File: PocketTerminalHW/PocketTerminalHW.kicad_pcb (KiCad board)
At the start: 2 copper layers, 85.5 x 54 mm, 183 parts, among them J1 USB4105-GF-A, J2 DM3D-SF, J3 53261-0271, J4 Conn_01x04, J5 Conn_01x02, J6 68712414522, J7 USB4105-GF-A, J8 66011102111302, J9 Conn_01x05, Q1 BC847BDW1, SW1 K3-1391D-5MM, U1 ESP32-S3-WROOM-1, U2 CP2102N-A02-GQFN28, U3 AMS1117-3.3 / SGM2212-3.3, U4 TP4056-42-ESOP8, U5 MT3608/SX1308, U6 CC1101RGPR, Y1 3225-26M-SR

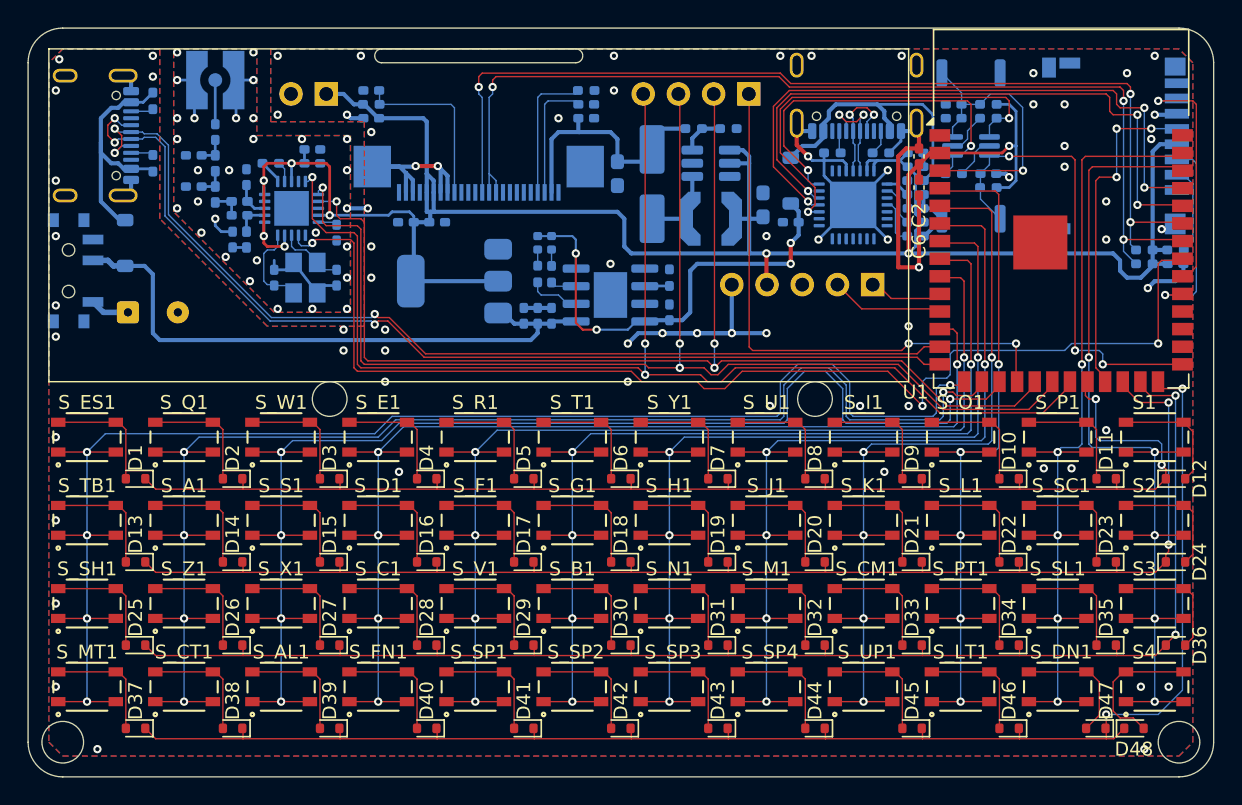
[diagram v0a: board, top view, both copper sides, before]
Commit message: Project rename and minor PCB changes
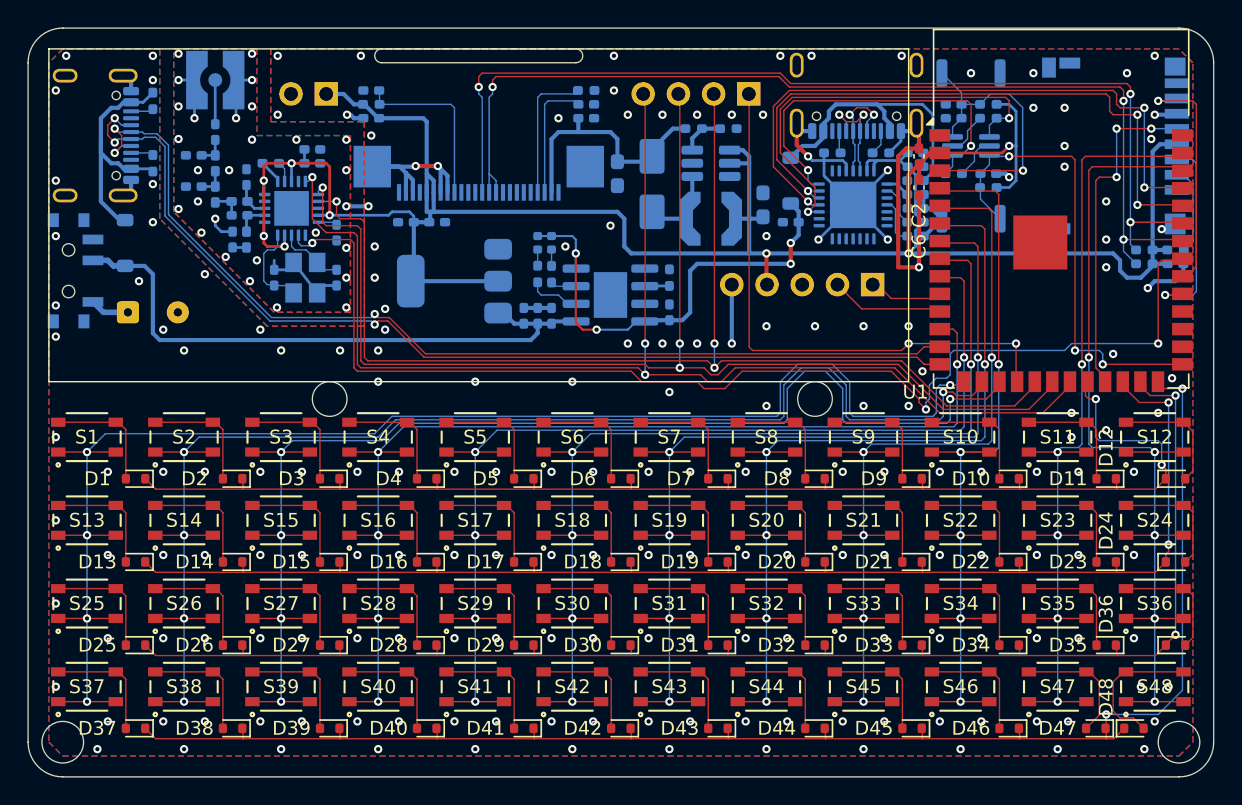
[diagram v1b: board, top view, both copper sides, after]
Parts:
- D52: footprint Diode_SMD:D_SMA_Handsoldering -> Diode_SMD:D_SMA
- J6: footprint DataSlice:68712414522 -> PocketTerminal:68712414522
- S1: renamed from S_ES1; footprint DataSlice:SW4_SKRPABE010_ALPS -> PocketTerminal:SW4_SKRPABE010_ALPS
- S10: renamed from S_O1; footprint DataSlice:SW4_SKRPABE010_ALPS -> PocketTerminal:SW4_SKRPABE010_ALPS
- S11: renamed from S_P1; footprint DataSlice:SW4_SKRPABE010_ALPS -> PocketTerminal:SW4_SKRPABE010_ALPS
- S12: renamed from S1; footprint DataSlice:SW4_SKRPABE010_ALPS -> PocketTerminal:SW4_SKRPABE010_ALPS
- S13: renamed from S_TB1; footprint DataSlice:SW4_SKRPABE010_ALPS -> PocketTerminal:SW4_SKRPABE010_ALPS
- S14: renamed from S_A1; footprint DataSlice:SW4_SKRPABE010_ALPS -> PocketTerminal:SW4_SKRPABE010_ALPS
- S15: renamed from S_S1; footprint DataSlice:SW4_SKRPABE010_ALPS -> PocketTerminal:SW4_SKRPABE010_ALPS
- S16: renamed from S_D1; footprint DataSlice:SW4_SKRPABE010_ALPS -> PocketTerminal:SW4_SKRPABE010_ALPS
- S17: renamed from S_F1; footprint DataSlice:SW4_SKRPABE010_ALPS -> PocketTerminal:SW4_SKRPABE010_ALPS
- S18: renamed from S_G1; footprint DataSlice:SW4_SKRPABE010_ALPS -> PocketTerminal:SW4_SKRPABE010_ALPS
- S19: renamed from S_H1; footprint DataSlice:SW4_SKRPABE010_ALPS -> PocketTerminal:SW4_SKRPABE010_ALPS
- S2: renamed from S_Q1; footprint DataSlice:SW4_SKRPABE010_ALPS -> PocketTerminal:SW4_SKRPABE010_ALPS
- S20: renamed from S_J1; footprint DataSlice:SW4_SKRPABE010_ALPS -> PocketTerminal:SW4_SKRPABE010_ALPS
- S21: renamed from S_K1; footprint DataSlice:SW4_SKRPABE010_ALPS -> PocketTerminal:SW4_SKRPABE010_ALPS
- S22: renamed from S_L1; footprint DataSlice:SW4_SKRPABE010_ALPS -> PocketTerminal:SW4_SKRPABE010_ALPS
- S23: renamed from S_SC1; footprint DataSlice:SW4_SKRPABE010_ALPS -> PocketTerminal:SW4_SKRPABE010_ALPS
- S24: renamed from S2; footprint DataSlice:SW4_SKRPABE010_ALPS -> PocketTerminal:SW4_SKRPABE010_ALPS
- S25: renamed from S_SH1; footprint DataSlice:SW4_SKRPABE010_ALPS -> PocketTerminal:SW4_SKRPABE010_ALPS
- S26: renamed from S_Z1; footprint DataSlice:SW4_SKRPABE010_ALPS -> PocketTerminal:SW4_SKRPABE010_ALPS
- S27: renamed from S_X1; footprint DataSlice:SW4_SKRPABE010_ALPS -> PocketTerminal:SW4_SKRPABE010_ALPS
- S28: renamed from S_C1; footprint DataSlice:SW4_SKRPABE010_ALPS -> PocketTerminal:SW4_SKRPABE010_ALPS
- S29: renamed from S_V1; footprint DataSlice:SW4_SKRPABE010_ALPS -> PocketTerminal:SW4_SKRPABE010_ALPS
- S3: renamed from S_W1; footprint DataSlice:SW4_SKRPABE010_ALPS -> PocketTerminal:SW4_SKRPABE010_ALPS
- S30: renamed from S_B1; footprint DataSlice:SW4_SKRPABE010_ALPS -> PocketTerminal:SW4_SKRPABE010_ALPS
- S31: renamed from S_N1; footprint DataSlice:SW4_SKRPABE010_ALPS -> PocketTerminal:SW4_SKRPABE010_ALPS
- S32: renamed from S_M1; footprint DataSlice:SW4_SKRPABE010_ALPS -> PocketTerminal:SW4_SKRPABE010_ALPS
- S33: renamed from S_CM1; footprint DataSlice:SW4_SKRPABE010_ALPS -> PocketTerminal:SW4_SKRPABE010_ALPS
- S34: renamed from S_PT1; footprint DataSlice:SW4_SKRPABE010_ALPS -> PocketTerminal:SW4_SKRPABE010_ALPS
- S35: renamed from S_SL1; footprint DataSlice:SW4_SKRPABE010_ALPS -> PocketTerminal:SW4_SKRPABE010_ALPS
- S36: renamed from S3; footprint DataSlice:SW4_SKRPABE010_ALPS -> PocketTerminal:SW4_SKRPABE010_ALPS
- S37: renamed from S_MT1; footprint DataSlice:SW4_SKRPABE010_ALPS -> PocketTerminal:SW4_SKRPABE010_ALPS
- S38: renamed from S_CT1; footprint DataSlice:SW4_SKRPABE010_ALPS -> PocketTerminal:SW4_SKRPABE010_ALPS
- S39: renamed from S_AL1; footprint DataSlice:SW4_SKRPABE010_ALPS -> PocketTerminal:SW4_SKRPABE010_ALPS
- S4: renamed from S_E1; footprint DataSlice:SW4_SKRPABE010_ALPS -> PocketTerminal:SW4_SKRPABE010_ALPS
- S40: renamed from S_FN1; footprint DataSlice:SW4_SKRPABE010_ALPS -> PocketTerminal:SW4_SKRPABE010_ALPS
- S41: renamed from S_SP1; footprint DataSlice:SW4_SKRPABE010_ALPS -> PocketTerminal:SW4_SKRPABE010_ALPS
- S42: renamed from S_SP2; footprint DataSlice:SW4_SKRPABE010_ALPS -> PocketTerminal:SW4_SKRPABE010_ALPS
- S43: renamed from S_SP3; footprint DataSlice:SW4_SKRPABE010_ALPS -> PocketTerminal:SW4_SKRPABE010_ALPS
- S44: renamed from S_SP4; footprint DataSlice:SW4_SKRPABE010_ALPS -> PocketTerminal:SW4_SKRPABE010_ALPS
- S45: renamed from S_UP1; footprint DataSlice:SW4_SKRPABE010_ALPS -> PocketTerminal:SW4_SKRPABE010_ALPS
- S46: renamed from S_LT1; footprint DataSlice:SW4_SKRPABE010_ALPS -> PocketTerminal:SW4_SKRPABE010_ALPS
- S47: renamed from S_DN1; footprint DataSlice:SW4_SKRPABE010_ALPS -> PocketTerminal:SW4_SKRPABE010_ALPS
- S48: renamed from S4; footprint DataSlice:SW4_SKRPABE010_ALPS -> PocketTerminal:SW4_SKRPABE010_ALPS
- S5: renamed from S_R1; footprint DataSlice:SW4_SKRPABE010_ALPS -> PocketTerminal:SW4_SKRPABE010_ALPS
- S6: renamed from S_T1; footprint DataSlice:SW4_SKRPABE010_ALPS -> PocketTerminal:SW4_SKRPABE010_ALPS
- S7: renamed from S_Y1; footprint DataSlice:SW4_SKRPABE010_ALPS -> PocketTerminal:SW4_SKRPABE010_ALPS
- S8: renamed from S_U1; footprint DataSlice:SW4_SKRPABE010_ALPS -> PocketTerminal:SW4_SKRPABE010_ALPS
- S9: renamed from S_I1; footprint DataSlice:SW4_SKRPABE010_ALPS -> PocketTerminal:SW4_SKRPABE010_ALPS
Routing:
- net GND: track 118.7 -> 101.5 mm, vias 102 -> 221

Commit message: Minor PCB adjustments, change charger to TP4057
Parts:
- D50: renamed from D51; moved to F.Cu
- D51: renamed from D50; moved to F.Cu
- R14: renamed from R15; moved to F.Cu
- R15: renamed from R14; moved to F.Cu
- R16: value 3K(1%) -> 2K(1%)
- U4: value TP4056-42-ESOP8 -> TP4057; footprint Package_SO:SOIC-8-1EP_3.9x4.9mm_P1.27mm_EP2.41x3.3mm_ThermalVias -> Package_TO_SOT_SMD:TSOT-23-6
- moved D50 14.1 mm to (106.5, 62.0), turned to 0 degrees
- moved C15 13.9 mm to (94.2, 49.2), turned to 0 degrees
- moved D51 11.5 mm to (99.5, 62.0), turned to 180 degrees
- moved R14 11.0 mm to (104.2, 62.0), turned to 180 degrees
- moved R15 10.2 mm to (101.8, 62.0), turned to 180 degrees
- moved R16 6.93 mm to (100.2, 50.2), turned to 0 degrees
- moved U4 5.71 mm to (97.2, 51.8), turned to 90 degrees
- moved C16 1.95 mm to (96.8, 54.5), turned to 180 degrees
- moved C10 0.90 mm to (96.8, 56.5), turned to 180 degrees
- moved C11 0.56 mm to (96.8, 55.5), turned to 0 degrees
- renumbered J9 to J3, J3 to J4, J4 to J5, J5 to J6, J6 to J7, J7 to J8, J8 to J9
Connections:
- D51 pad 1: Net-(D50-K) (its old number) -> Net-(D51-K)
- R15 pad 1: Net-(D50-K) (its old number) -> Net-(U4-STDBY)
- R15 pad 2: Net-(U4-~{STDBY}) -> Net-(D51-K)
- U4 pad 1: GND -> Net-(U4-~{CHRG})
- U4 pad 2: Net-(U4-PROG) -> GND
- U4 pad 3: GND -> +BATT
- U4 pad 5: +BATT -> Net-(U4-STDBY)
- U4 pad 6: Net-(U4-~{STDBY}) -> Net-(U4-PROG)
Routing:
- net +5V: track 34.2 -> 51.2 mm, vias 4 -> 5
- net Net-(U4-STDBY): track 0.00 -> 15.9 mm, vias 0 -> 3
- net Net-(U4-~{CHRG}): track 1.89 -> 16.4 mm, vias 0 -> 3
- net GND: track 101.5 -> 108.9 mm, vias 221 -> 219
- net Net-(U4-~{STDBY}): track 3.81 -> 0.00 mm
- net Net-(D51-K): track 0.00 -> 1.17 mm
- net Net-(D50-K) (its old number): track 1.17 -> 0.00 mm
- net +BATT: track 43.8 -> 42.9 mm

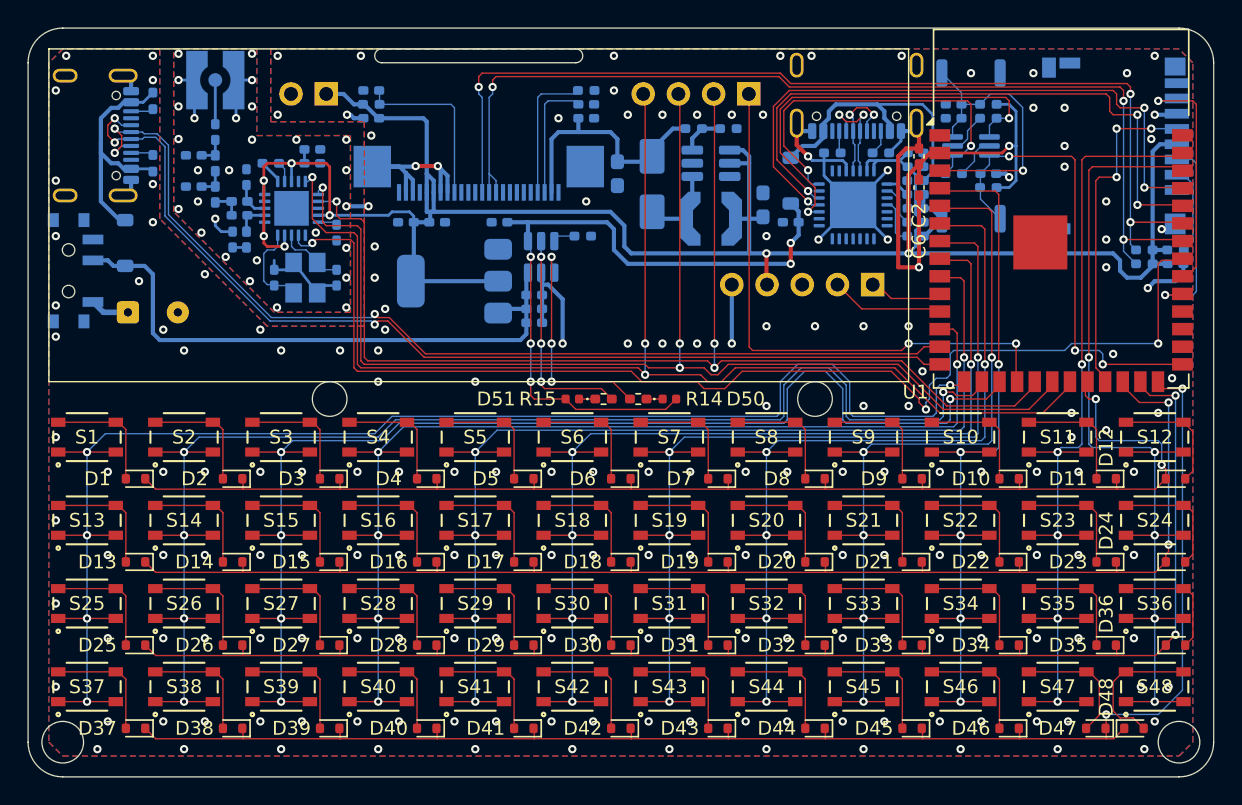
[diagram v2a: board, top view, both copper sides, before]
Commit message: Moved mounting holes
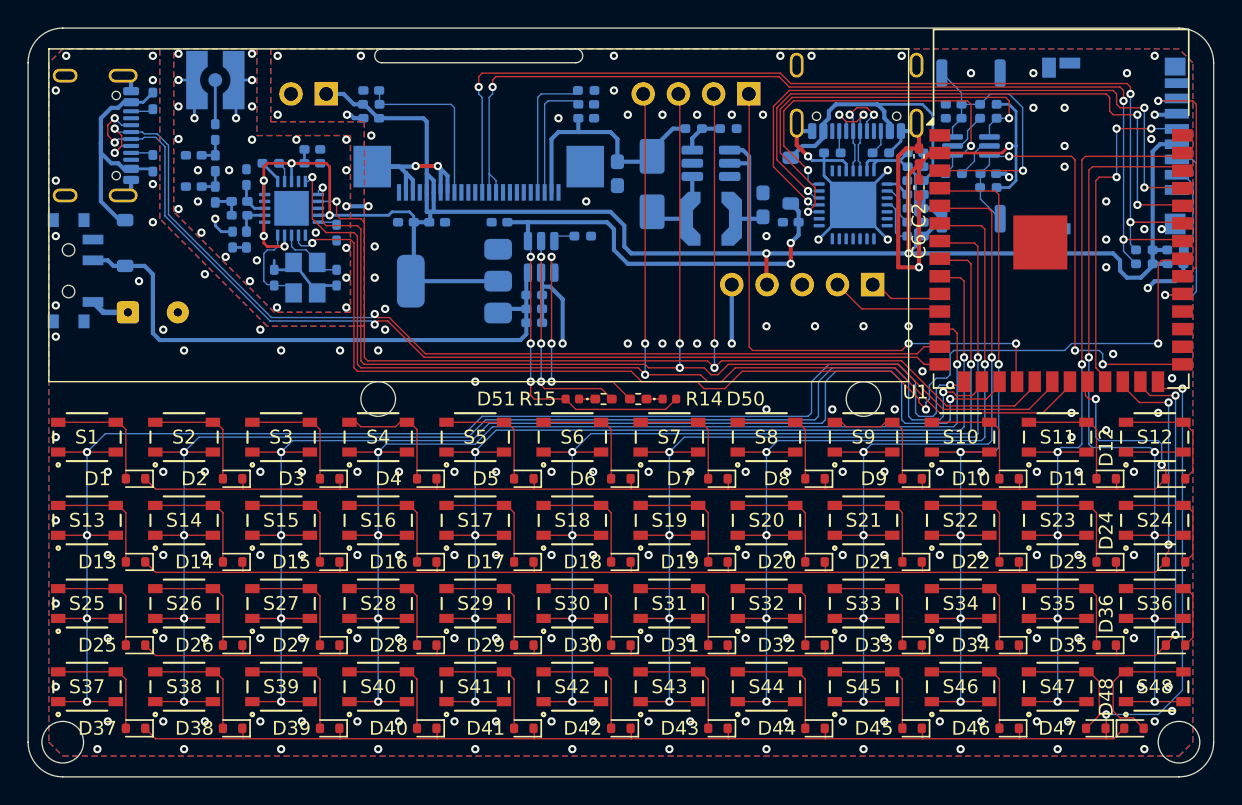
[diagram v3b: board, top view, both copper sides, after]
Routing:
- net GND: track 108.9 -> 108.2 mm, vias 219 -> 220
- net /KB_C_2: track 95.3 -> 95.9 mm
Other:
- outline, holes or cut-outs redrawn
